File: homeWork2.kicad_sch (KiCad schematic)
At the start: 37 parts, among them J3 Barrel_Jack_Switch_SMT, J4 0.100_2Pin, J5 0.100_2Pin, U1 LM7805_TO220

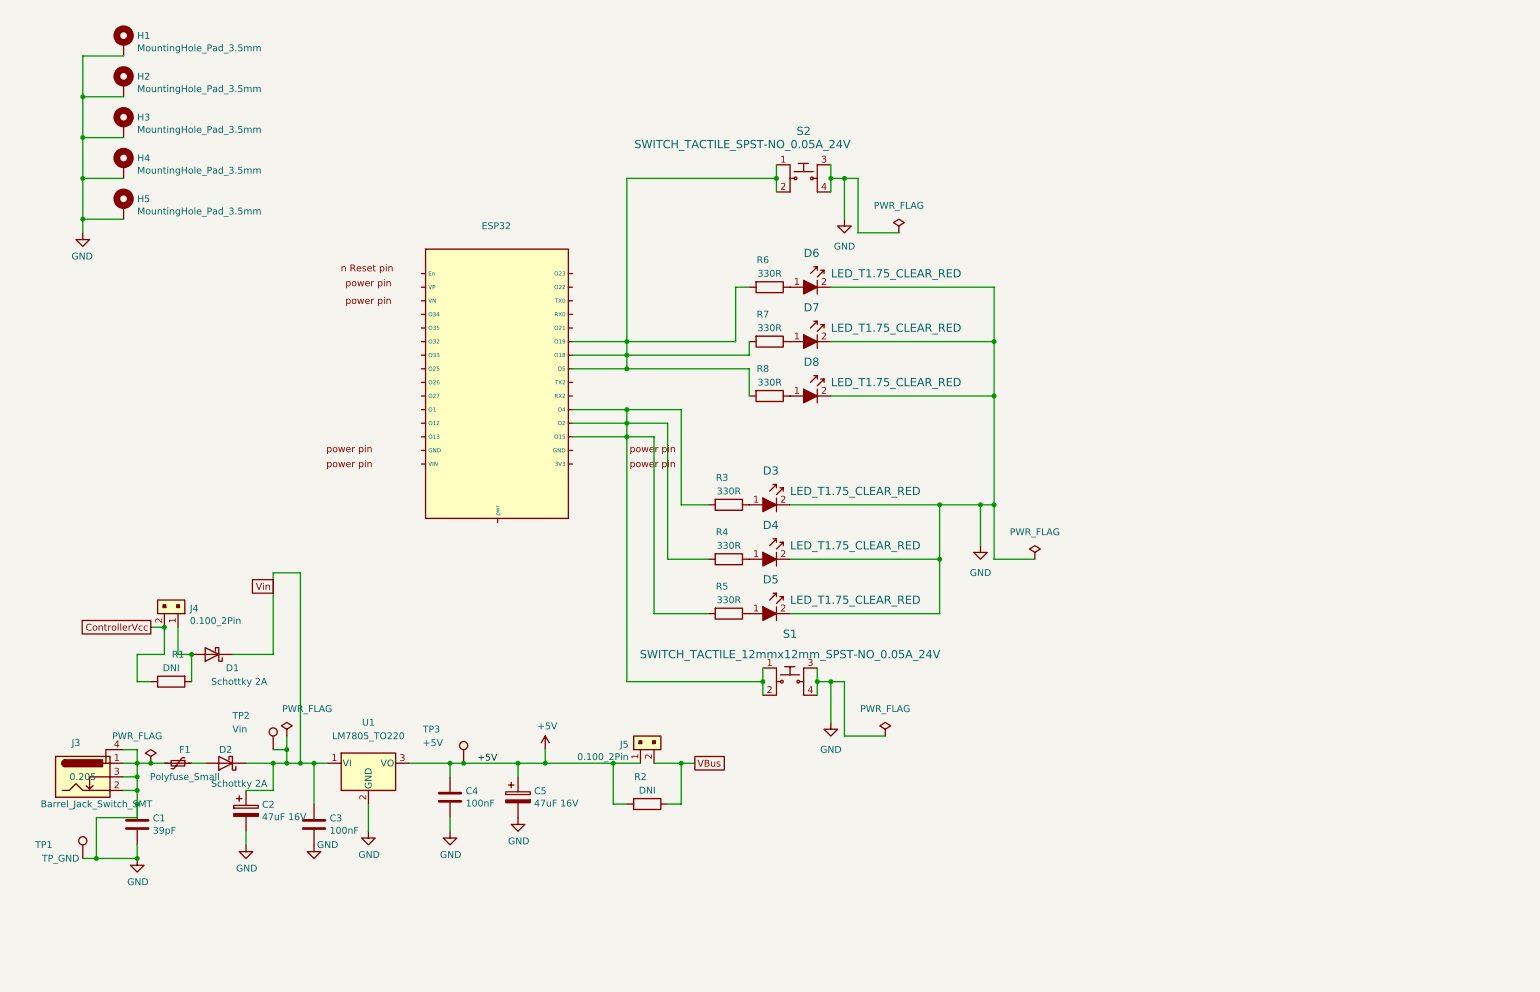
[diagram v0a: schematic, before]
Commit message: Schematic changes
the ESP32 symbol library is not saved in the same folder of the project and linked to the footprint library
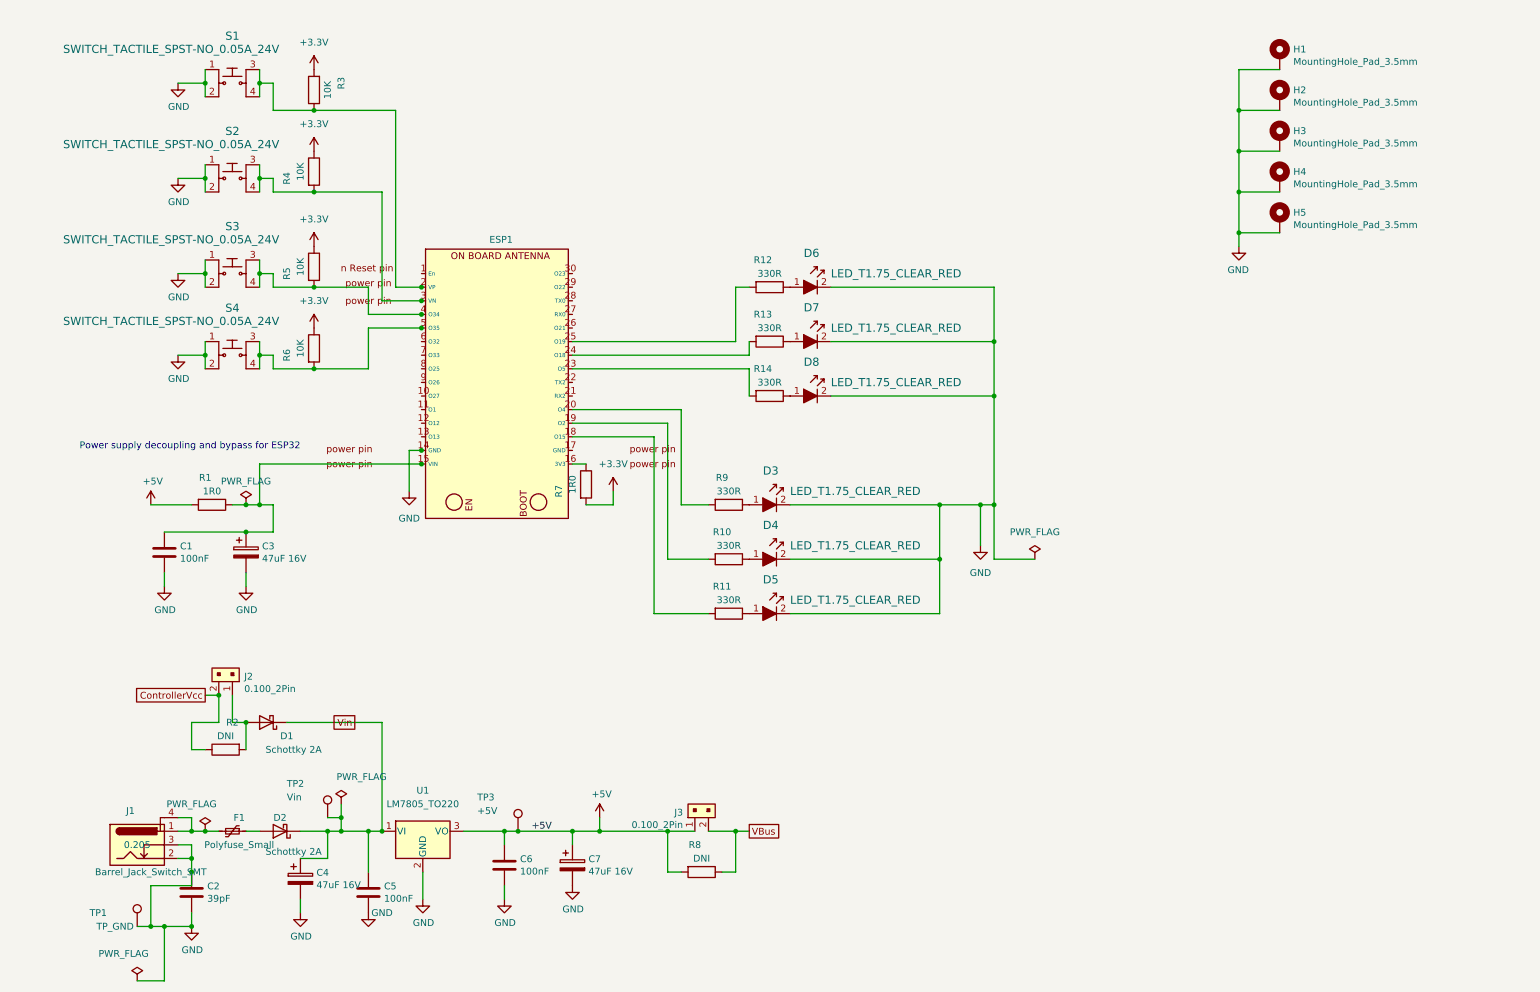
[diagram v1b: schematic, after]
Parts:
- removed ESP32: ~, esp32 15 pin Library:esp32, symbol New_Library.ESP32KIT:ESP32
- removed S1: SWITCH_TACTILE_12mmx12mm_SPST-NO_0.05A_24V, PubInv_KiCad_PCB:SW_PUSH-12mm_WithCap_Green, symbol GPAD_SCH_LIB:SWITCH_TACTILE_12mmx12mm_SPST-NO_0.05A_24V
- added C1: 100nF, Capacitor_SMD:C_0603_1608Metric_Pad1.08x0.95mm_HandSolder, symbol Device:C
- added C3: 47uF 16V, Capacitor_SMD:CP_Elec_5x5.4, symbol Device:C_Polarized
- added ESP1: ~, esp32 15 pin Library:esp32, symbol New_Library.ESP32KIT:ESP32_-_V2
- added R1, R7: 1R0, Resistor_SMD:R_0603_1608Metric_Pad0.98x0.95mm_HandSolder, symbol Device:R
- added R3, R4, R5, R6: 10K, Resistor_SMD:R_0603_1608Metric_Pad0.98x0.95mm_HandSolder, symbol Device:R
- added S2, S3, S4: SWITCH_TACTILE_SPST-NO_0.05A_24V, PubInv_KiCad_PCB:Switch_Tactile_THT_6x6mm, symbol GPAD_SCH_LIB:SWITCH_TACTILE_SPST-NO_0.05A_24V
- J1: renamed from J3; footprint GeneralPurposeAlarmDevicePCB:BarrelJack_CLIFF_FC681465S_SMT_Horizontal -> PubInv_KiCad_PCB:BarrelJack_CLIFF_FC681465S_SMT_Horizontal
- renumbered C1 to C2, C2 to C4, C3 to C5, C4 to C6, C5 to C7, J4 to J2, J5 to J3, R4 to R10, R5 to R11, R6 to R12, R7 to R13, R8 to R14, R1 to R2, R2 to R8, R3 to R9, S2 to S1
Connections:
- net +5V: now also R1.2
- net GND: now also S1.1, S1.2, C1.2, C3.2, ESP1.14 (GND), S2.1, S2.2, S3.1, S3.2, S4.1, S4.2; no longer F1.2, J1.1, J1.4, S1.3, S1.4
- new net: ESP1.19 (O2), R10.2
- new net: C1.1, C3.1, ESP1.15 (VIN), R1.1
- new net: ESP1.16 (3V3), R7.1
- new net: ESP1.18 (O15), R11.2
- new net: ESP1.2 (VP), R3.1, S1.3, S1.4
- new net: ESP1.20 (O4), R9.2
- new net: ESP1.23 (O5), R14.2
- new net: ESP1.24 (O18), R13.2
- new net: ESP1.25 (O19), R12.2
- new net: ESP1.3 (VN), R4.2, S2.3, S2.4
- new net: ESP1.4 (O34), R5.2, S3.3, S3.4
- new net: ESP1.5 (O35), R6.2, S4.3, S4.4
- new net: F1.2, J1.1, J1.4
- new net +3.3V: R3.2, R4.1, R5.1, R6.1, R7.2
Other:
- note added: "Power supply decoupling and bypass for ESP32"
- moved on the sheet: C2, C4, C5, C6, C7, D1, D2, F1, H1, H2, H3, H4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

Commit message: PCB Update
Copper routing PCB components
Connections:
- net GND: now also ESP1.17 (GND); no longer ESP1.14 (GND)
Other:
- company: (none) -> Public Invention Supervision
- title: (none) -> Esp32-6leds-4switches-2pj-circuit
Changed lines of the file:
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@@
 (kicad_sch (version 20230121) (generator eeschema)
   (paper "A4")
+  (title_block
+    (title "Esp32-6leds-4switches-2pj-circuit")
+    (date "2024-04-14")
+    (rev "V2")
+    (company "Public Invention Supervision")
+    (comment 1 "Coordinator: Robert Read")
+    (comment 2 "Mentor: Forest Lee Ereckson")
+    (comment 3 "Done by: Nagham Kheir")
+  )
   (junction (at 55.88 43.18) (diameter 0) (color 0 0 0 0)
   )
@@
   (junction (at 132.08 165.1) (diameter 0) (color 0 0 0 0)
   )
+  (junction (at 40.64 76.2) (diameter 0) (color 0 0 0 0)
+  )
   (junction (at 48.26 139.7) (diameter 0) (color 0 0 0 0)
   )
+  (junction (at 40.64 25.4) (diameter 0) (color 0 0 0 0)
+  )
   (junction (at 193.04 73.66) (diameter 0) (color 0 0 0 0)
   )
@@
   (junction (at 78.74 165.1) (diameter 0) (color 0 0 0 0)
   )
+  (junction (at 40.64 43.18) (diameter 0) (color 0 0 0 0)
+  )
   (junction (at 68.58 165.1) (diameter 0) (color 0 0 0 0)
   )
@@
   (junction (at 45.72 60.96) (diameter 0) (color 0 0 0 0)
   )
-  (junction (at 86.106 93.98) (diameter 0) (color 0 0 0 0)
-  )
   (junction (at 55.88 104.14) (diameter 0) (color 0 0 0 0)
   )
@@
   (junction (at 182.88 114.3) (diameter 0) (color 0 0 0 0)
   )
+  (junction (at 40.64 60.96) (diameter 0) (color 0 0 0 0)
+  )
   (junction (at 55.88 25.4) (diameter 0) (color 0 0 0 0)
   )
@@
     (stroke (width 0) (type default))
   )
-  (wire (pts (xy 86.106 93.98) (xy 83.82 93.98))
-    (stroke (width 0) (type default))
-  )
   (wire (pts (xy 144.78 172.72) (xy 144.78 165.1))
     (stroke (width 0) (type default))
@@
     (stroke (width 0) (type default))
   )
-  (wire (pts (xy 86.36 93.98) (xy 86.106 93.98))
-    (stroke (width 0) (type default))
-  )
   (wire (pts (xy 132.08 114.3) (xy 139.7 114.3))
     (stroke (width 0) (type default))
@@
     (stroke (width 0) (type default))
   )
-  (wire (pts (xy 83.82 93.98) (xy 83.82 101.6))
-    (stroke (width 0) (type default))
-  )
   (wire (pts (xy 45.72 43.18) (xy 45.72 45.72))
     (stroke (width 0) (type default))
@@
     (stroke (width 0) (type default))
   )
+  (wire (pts (xy 114.3 93.98) (xy 119.38 93.98))
+    (stroke (width 0) (type default))
+  )
   (wire (pts (xy 58.42 78.74) (xy 66.04 78.74))
     (stroke (width 0) (type default))
@@
     )
   )
+  (symbol (lib_id "power:GND") (at 119.38 93.98 0) (mirror y) (unit 1)
+    (in_bom yes) (on_board yes) (dnp no) (fields_autoplaced)
+    (property "Reference" "#PWR023" (at 119.38 100.33 0)
+      (effects (font (size 1.27 1.27)) hide)
+    )
+    (property "Value" "GND" (at 119.38 99.06 0)
+      (effects (font (size 1.27 1.27)))
+    )
+    (property "Footprint" "" (at 119.38 93.98 0)
+      (effects (font (size 1.27 1.27)) hide)
+    )
+    (property "Datasheet" "" (at 119.38 93.98 0)
+      (effects (font (size 1.27 1.27)) hide)
+    )
+    (pin "1")
+    (instances
+      (project "homeWork2"
+        (path "/0dd285f0-5d03-432a-a2cf-fee3b00868c5"
+          (reference "#PWR023") (unit 1)
+        )
+      )
+    )
+  )
   (symbol (lib_id "Device:C") (at 101.6 171.45 0) (unit 1)
     (in_bom yes) (on_board yes) (dnp no)
@@
       (effects (font (size 1.27 1.27)) hide)
     )
-    (pin "16")
-    (pin "14")
-    (pin "17")
+    (pin "1")
+    (pin "10")
     (pin "11")
     (pin "12")
     (pin "13")
+    (pin "14")
+    (pin "15")
+    (pin "16")
+    (pin "17")
     (pin "18")
+    (pin "19")
+    (pin "2")
+    (pin "20")
+    (pin "21")
+    (pin "22")
+    (pin "23")
     (pin "24")
     (pin "25")
-    (pin "19")
     (pin "26")
+    (pin "27")
+    (pin "28")
     (pin "29")
+    (pin "3")
     (pin "30")
-    (pin "8")
-    (pin "9")
-    (pin "10")
-    (pin "6")
-    (pin "7")
     (pin "4")
     (pin "5")
-    (pin "20")
-    (pin "23")
-    (pin "27")
-    (pin "21")
-    (pin "28")
-    (pin "22")
-    (pin "15")
-    (pin "1")
-    (pin "2")
-    (pin "3")
+    (pin "6")
+    (pin "7")
+    (pin "8")
+    (pin "9")
     (instances
       (project "homeWork2"
@@
     )
   )
-  (symbol (lib_id "power:GND") (at 83.82 101.6 0) (mirror y) (unit 1)
-    (in_bom yes) (on_board yes) (dnp no) (fields_autoplaced)
-    (property "Reference" "#PWR015" (at 83.82 107.95 0)
-      (effects (font (size 1.27 1.27)) hide)
-    )
-    (property "Value" "GND" (at 83.82 106.68 0)
-      (effects (font (size 1.27 1.27)))
-    )
-    (property "Footprint" "" (at 83.82 101.6 0)
-      (effects (font (size 1.27 1.27)) hide)
-    )
-    (property "Datasheet" "" (at 83.82 101.6 0)
-      (effects (font (size 1.27 1.27)) hide)
-    )
-    (pin "1")
-    (instances
-      (project "homeWork2"
-        (path "/0dd285f0-5d03-432a-a2cf-fee3b00868c5"
-          (reference "#PWR015") (unit 1)
-        )
-      )
-    )
-  )
   (symbol (lib_id "Device:R") (at 66.04 74.93 0) (unit 1)
     (in_bom yes) (on_board yes) (dnp no)
@@
     )
   )
+  (symbol (lib_id "power:PWR_FLAG") (at 40.64 76.2 0) (unit 1)
+    (in_bom yes) (on_board yes) (dnp no)
+    (property "Reference" "#FLG06" (at 40.64 74.295 0)
+      (effects (font (size 1.27 1.27)) hide)
+    )
+    (property "Value" "PWR_FLAG" (at 40.64 71.8058 0)
+      (effects (font (size 1.27 1.27)))
+    )
+    (property "Footprint" "" (at 40.64 76.2 0)
+      (effects (font (size 1.27 1.27)) hide)
+    )
+    (property "Datasheet" "~" (at 40.64 76.2 0)
+      (effects (font (size 1.27 1.27)) hide)
+    )
+    (pin "1")
+    (instances
+      (project "homeWork2"
+        (path "/0dd285f0-5d03-432a-a2cf-fee3b00868c5"
+          (reference "#FLG06") (unit 1)
+        )
+      )
+      (project "GeneralPurposeAlarmDevicePCB"
+        (path "/412a327d-1ee3-473e-bc00-1545004b7edf"
+          (reference "#FLG0103") (unit 1)
+        )
+      )
+    )
+  )
   (symbol (lib_id "Device:R") (at 138.43 172.72 270) (unit 1)
     (in_bom yes) (on_board yes) (dnp no)
@@
     )
   )
+  (symbol (lib_id "power:PWR_FLAG") (at 40.64 60.96 0) (unit 1)
+    (in_bom yes) (on_board yes) (dnp no)
+    (property "Reference" "#FLG07" (at 40.64 59.055 0)
+      (effects (font (size 1.27 1.27)) hide)
+    )
+    (property "Value" "PWR_FLAG" (at 40.64 56.5658 0)
+      (effects (font (size 1.27 1.27)))
+    )
+    (property "Footprint" "" (at 40.64 60.96 0)
+      (effects (font (size 1.27 1.27)) hide)
+    )
+    (property "Datasheet" "~" (at 40.64 60.96 0)
+      (effects (font (size 1.27 1.27)) hide)
+    )
+    (pin "1")
+    (instances
+      (project "homeWork2"
+        (path "/0dd285f0-5d03-432a-a2cf-fee3b00868c5"
+          (reference "#FLG07") (unit 1)
+        )
+      )
+      (project "GeneralPurposeAlarmDevicePCB"
+        (path "/412a327d-1ee3-473e-bc00-1545004b7edf"
+          (reference "#FLG0103") (unit 1)
+        )
+      )
+    )
+  )
   (symbol (lib_id "power:GND") (at 43.18 182.88 0) (unit 1)
     (in_bom yes) (on_board yes) (dnp no)
@@
     )
   )
+  (symbol (lib_id "power:PWR_FLAG") (at 40.64 43.18 0) (unit 1)
+    (in_bom yes) (on_board yes) (dnp no)
+    (property "Reference" "#FLG08" (at 40.64 41.275 0)
+      (effects (font (size 1.27 1.27)) hide)
+    )
+    (property "Value" "PWR_FLAG" (at 40.64 38.7858 0)
+      (effects (font (size 1.27 1.27)))
+    )
+    (property "Footprint" "" (at 40.64 43.18 0)
+      (effects (font (size 1.27 1.27)) hide)
+    )
+    (property "Datasheet" "~" (at 40.64 43.18 0)
+      (effects (font (size 1.27 1.27)) hide)
+    )
+    (pin "1")
+    (instances
+      (project "homeWork2"
+        (path "/0dd285f0-5d03-432a-a2cf-fee3b00868c5"
+          (reference "#FLG08") (unit 1)
+        )
+      )
+      (project "GeneralPurposeAlarmDevicePCB"
+        (path "/412a327d-1ee3-473e-bc00-1545004b7edf"
+          (reference "#FLG0103") (unit 1)
+        )
+      )
+    )
+  )
   (symbol (lib_id "Device:R") (at 143.51 124.46 270) (unit 1)
     (in_bom yes) (on_board yes) (dnp no)
@@
         )
       )
+    )
+  )
+  (symbol (lib_id "power:PWR_FLAG") (at 40.64 25.4 0) (unit 1)
+    (in_bom yes) (on_board yes) (dnp no)
+    (property "Reference" "#FLG09" (at 40.64 23.495 0)
+      (effects (font (size 1.27 1.27)) hide)
+    )
+    (property "Value" "PWR_FLAG" (at 40.64 21.0058 0)
+      (effects (font (size 1.27 1.27)))
+    )
+    (property "Footprint" "" (at 40.64 25.4 0)
+      (effects (font (size 1.27 1.27)) hide)
+    )
+    (property "Datasheet" "~" (at 40.64 25.4 0)
+      (effects (font (size 1.27 1.27)) hide)
+    )
+    (pin "1")
+    (instances
+      (project "homeWork2"
+        (path "/0dd285f0-5d03-432a-a2cf-fee3b00868c5"
+          (reference "#FLG09") (unit 1)
+        )
+      )
+      (project "GeneralPurposeAlarmDevicePCB"
+        (path "/412a327d-1ee3-473e-bc00-1545004b7edf"
+          (reference "#FLG0103") (unit 1)
+        )
+      )
